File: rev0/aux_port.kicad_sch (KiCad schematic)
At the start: 21 parts, among them IC1 ECP5-BGA256, U11 USB3343-CP

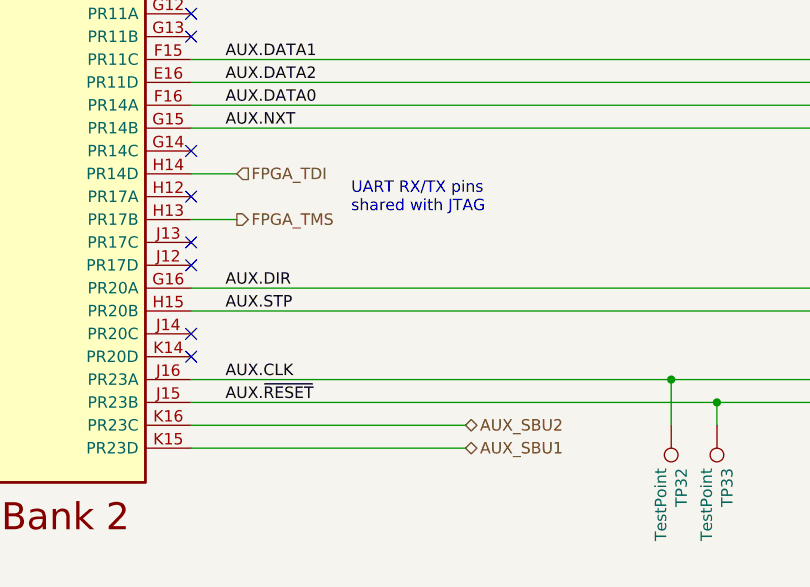
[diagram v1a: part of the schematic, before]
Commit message: hardware: replace power input diodes
- provide input selection capability with FETs
- reduce reverse leakage current
- provide overvoltage protection
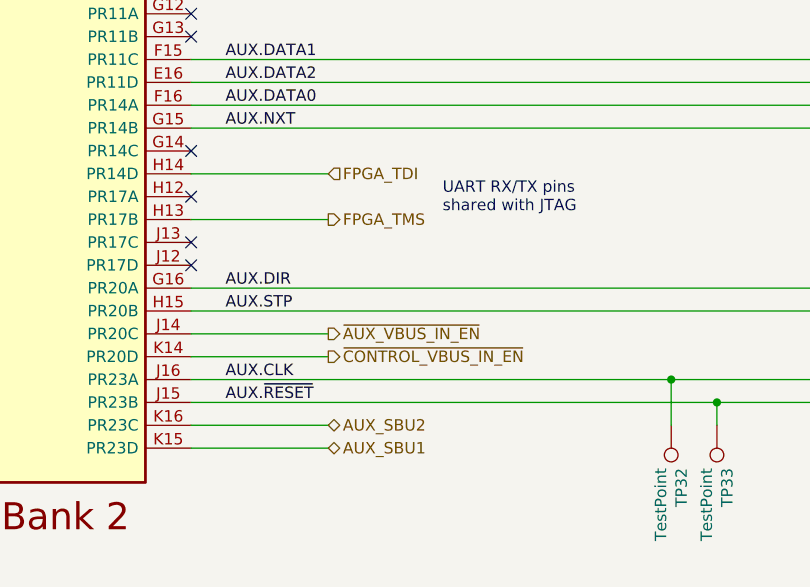
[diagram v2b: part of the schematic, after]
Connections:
- net ~{AUX_VBUS_IN_EN}: now reaches IC1.J14 (PR20C)
- net ~{CONTROL_VBUS_IN_EN}: now reaches IC1.K14 (PR20D)
- no-connect marks 14 -> 12
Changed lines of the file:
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@@
   (no_connect (at 59.69 95.25))
   (no_connect (at 59.69 115.57))
-  (no_connect (at 59.69 130.81))
   (no_connect (at 59.69 72.39))
   (no_connect (at 59.69 120.65))
   (no_connect (at 59.69 82.55))
-  (no_connect (at 59.69 133.35))
   (no_connect (at 59.69 123.19))
   (no_connect (at 227.33 87.63))
@@
     (stroke (width 0) (type default) (color 0 0 0 0))
   )
-  (wire (pts (xy 90.17 140.97) (xy 59.69 140.97))
+  (wire (pts (xy 74.93 140.97) (xy 59.69 140.97))
     (stroke (width 0) (type default) (color 0 0 0 0))
   )
@@
     (stroke (width 0) (type default) (color 0 0 0 0))
   )
+  (wire (pts (xy 74.93 133.35) (xy 59.69 133.35))
+    (stroke (width 0) (type default) (color 0 0 0 0))
+  )
   (bus (pts (xy 148.59 82.55) (xy 148.59 83.82))
     (stroke (width 0) (type default) (color 0 0 0 0))
@@
     (stroke (width 0) (type default) (color 0 0 0 0))
   )
-  (wire (pts (xy 59.69 118.11) (xy 64.77 118.11))
+  (wire (pts (xy 59.69 118.11) (xy 74.93 118.11))
     (stroke (width 0) (type default) (color 0 0 0 0))
   )
@@
     (stroke (width 0) (type default) (color 0 0 0 0))
   )
-  (wire (pts (xy 59.69 143.51) (xy 90.17 143.51))
+  (wire (pts (xy 59.69 143.51) (xy 74.93 143.51))
     (stroke (width 0) (type default) (color 0 0 0 0))
   )
@@
     (stroke (width 0) (type default) (color 0 0 0 0))
   )
+  (wire (pts (xy 59.69 130.81) (xy 74.93 130.81))
+    (stroke (width 0) (type default) (color 0 0 0 0))
+  )
   (wire (pts (xy 238.76 135.89) (xy 238.76 138.43))
     (stroke (width 0) (type default) (color 0 0 0 0))
@@
     (stroke (width 0) (type default) (color 0 0 0 0))
   )
-  (wire (pts (xy 64.77 113.03) (xy 59.69 113.03))
+  (wire (pts (xy 74.93 113.03) (xy 59.69 113.03))
     (stroke (width 0) (type default) (color 0 0 0 0))
   )
@@
     (stroke (width 0) (type default) (color 0 0 0 0))
   )
-  (text "UART RX/TX pins\nshared with JTAG" (at 77.47 117.475 0)
+  (text "UART RX/TX pins\nshared with JTAG" (at 87.63 117.475 0)
     (effects (font (size 1.27 1.27)) (justify left bottom))
   )
@@
     (effects (font (size 1.27 1.27)) (justify right bottom))
   )
-  (hierarchical_label "FPGA_TMS" (shape output) (at 64.77 118.11 0)
+  (hierarchical_label "FPGA_TMS" (shape output) (at 74.93 118.11 0)
     (effects (font (size 1.27 1.27)) (justify left))
   )
@@
     (effects (font (size 1.27 1.27)) (justify left))
   )
-  (hierarchical_label "AUX_SBU1" (shape bidirectional) (at 90.17 143.51 0)
+  (hierarchical_label "AUX_SBU1" (shape bidirectional) (at 74.93 143.51 0)
+    (effects (font (size 1.27 1.27)) (justify left))
+  )
+  (hierarchical_label "~{AUX_VBUS_IN_EN}" (shape output) (at 74.93 130.81 0)
     (effects (font (size 1.27 1.27)) (justify left))
   )
@@
     (effects (font (size 1.27 1.27)) (justify left))
   )
-  (hierarchical_label "AUX_SBU2" (shape bidirectional) (at 90.17 140.97 0)
-    (effects (font (size 1.27 1.27)) (justify left))
-  )
-  (hierarchical_label "FPGA_TDI" (shape input) (at 64.77 113.03 0)
-    (effects (font (size 1.27 1.27)) (justify left))
-  )
+  (hierarchical_label "AUX_SBU2" (shape bidirectional) (at 74.93 140.97 0)
+    (effects (font (size 1.27 1.27)) (justify left))
+  )
+  (hierarchical_label "~{CONTROL_VBUS_IN_EN}" (shape output) (at 74.93 133.35 0)
+    (effects (font (size 1.27 1.27)) (justify left))
+  )
+  (hierarchical_label "FPGA_TDI" (shape input) (at 74.93 113.03 0)
+    (effects (font (size 1.27 1.27)) (justify left))
+  )

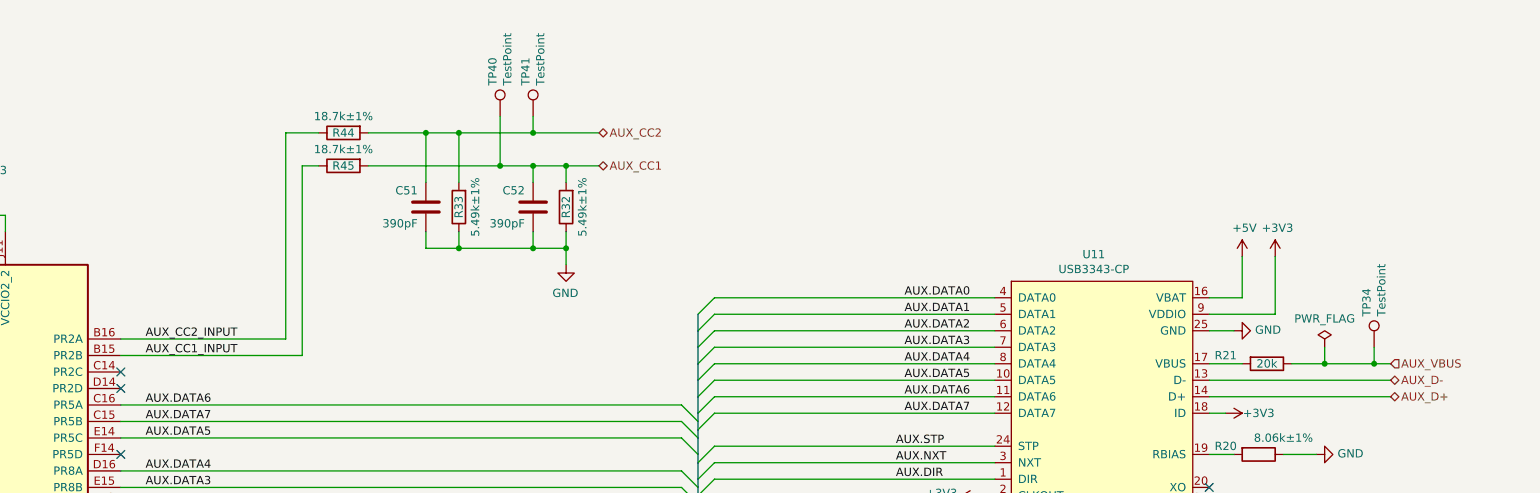
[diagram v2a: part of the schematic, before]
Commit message: hardware: add Aux port Type-C controller
replaces rudimentary CC pin input
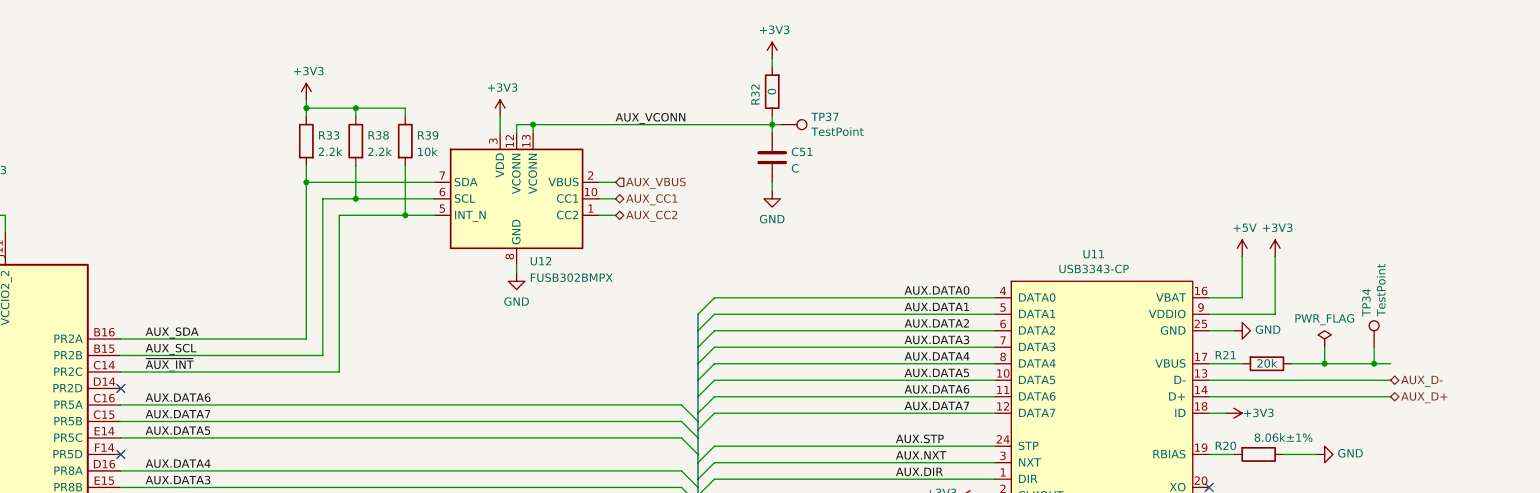
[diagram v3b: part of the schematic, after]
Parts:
- removed C52: 390pF, Capacitor_SMD:C_0402_1005Metric, symbol Device:C
- removed R44, R45: 18.7k±1%, Resistor_SMD:R_0402_1005Metric, symbol Device:R
- removed TP40, TP41: TestPoint, TestPoint:TestPoint_Pad_D1.0mm, symbol Connector:TestPoint
- added R38: 2.2k, Resistor_SMD:R_0402_1005Metric, symbol Device:R
- added R39: 10k, Resistor_SMD:R_0402_1005Metric, symbol Device:R
- added TP37: TestPoint, TestPoint:TestPoint_Pad_D1.0mm, symbol Connector:TestPoint
- added U12: FUSB302BMPX, Package_DFN_QFN:WQFN-14-1EP_2.5x2.5mm_P0.5mm_EP1.45x1.45mm, symbol Interface_USB:FUSB302BMPX
- C51: value 390pF -> C; Part Number GENERIC-CAP-0402-390pF -> (none); Substitution any equivalent -> (none)
- R32: value 5.49k±1% -> 0; Manufacturer Panasonic -> (none); Part Number ERJ-2RKF5491X -> GENERIC-RES-0402-0
- R33: value 5.49k±1% -> 2.2k; Manufacturer Panasonic -> (none); Part Number ERJ-2RKF5491X -> GENERIC-RES-0402-2.2K
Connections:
- net +3V3: now also R32.2, R33.1, R38.1, R39.1, U12.3 (VDD), U12.4 (VDD)
- net AUX_CC1: now also U12.10 (CC1), U12.11 (CC1); no longer R32.2
- net AUX_CC2: now also U12.1 (CC2), U12.14 (CC2); no longer C51.1, R33.2
- net AUX_VBUS: now also U12.2 (VBUS); no longer R21.1, TP34.1
- net GND: now also U12.15 (GND), U12.8 (GND), U12.9 (GND); no longer R32.1, R33.1
- net ~{AUX_INT}: now reaches IC1.C14 (PR2C)
- net ~{AUX_INT}: now also R39.2, U12.5 (INT_N)
- net AUX_CC1_INPUT renamed AUX_SCL
- net AUX_SCL: now also R38.2, U12.6 (SCL)
- net AUX_CC2_INPUT renamed AUX_SDA
- net AUX_SDA: now also R33.2, U12.7 (SDA)
- new net: R21.1, TP34.1
- new net AUX_VCONN: C51.1, R32.1, TP37.1, U12.12 (VCONN), U12.13 (VCONN)
- no-connect marks 12 -> 11

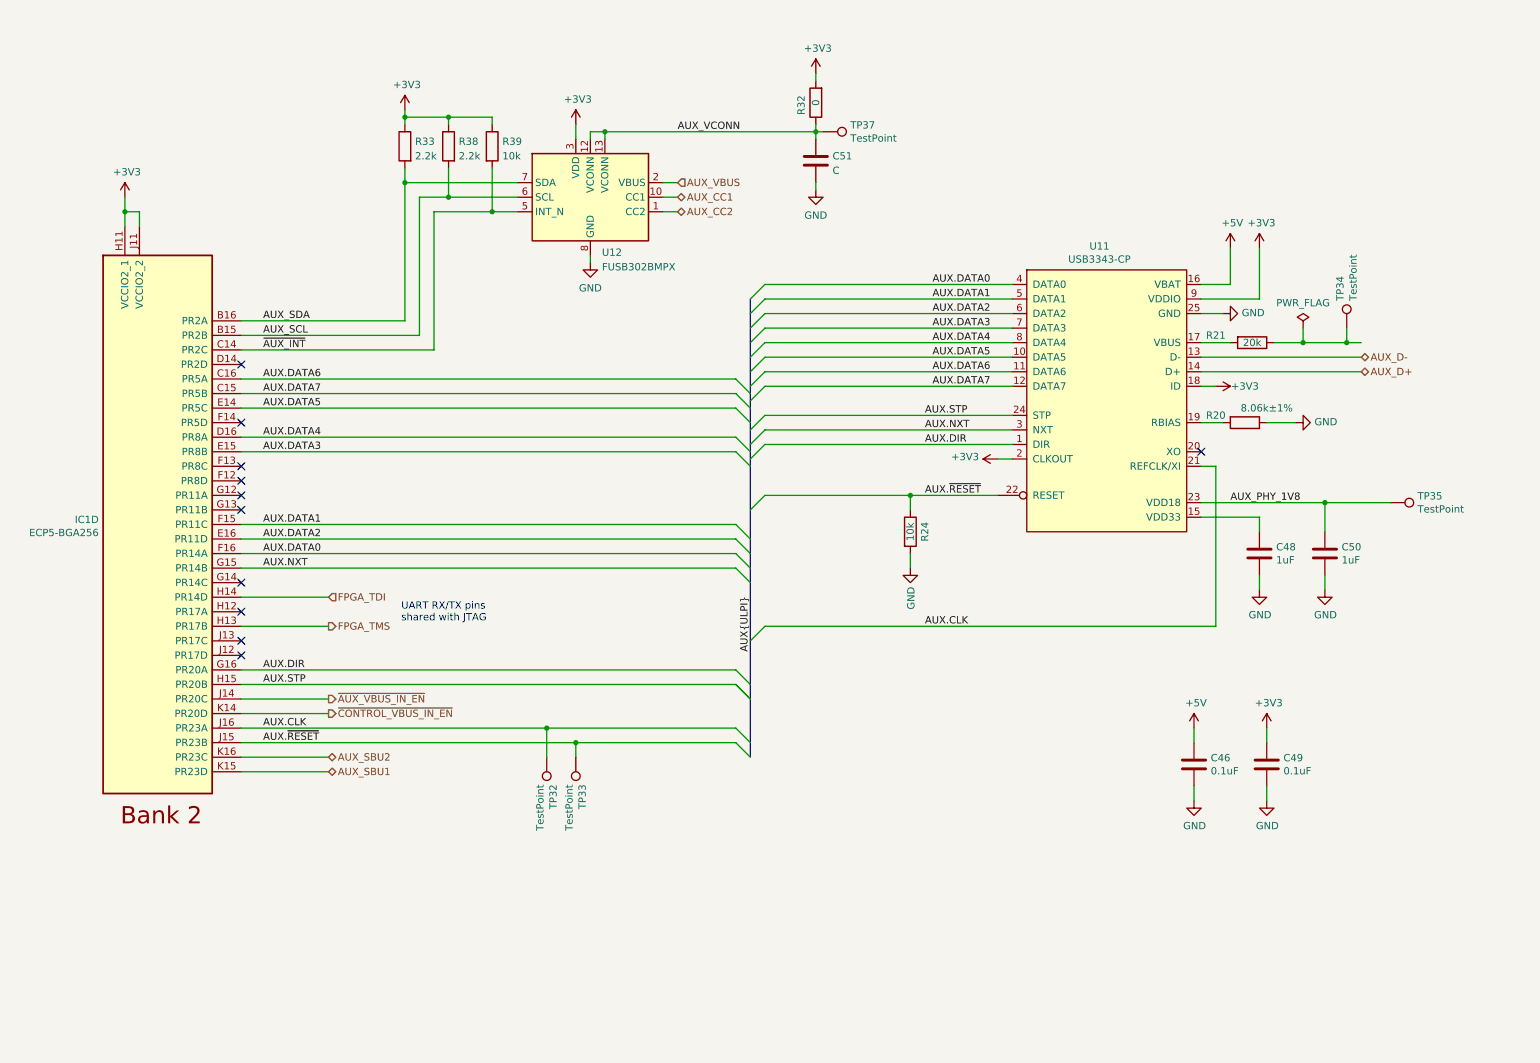
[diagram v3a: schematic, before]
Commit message: hardware: simplify Control port Type-C connections
- remove CC/FPGA connections to ensure correct Rd is reliably present
- remove SBU/FPGA connections to avoid need for ESD protection

We provide CC and SBU pin access on the Target and Aux port. They are
not necessary on the Control port. Simplification ensures reliability.
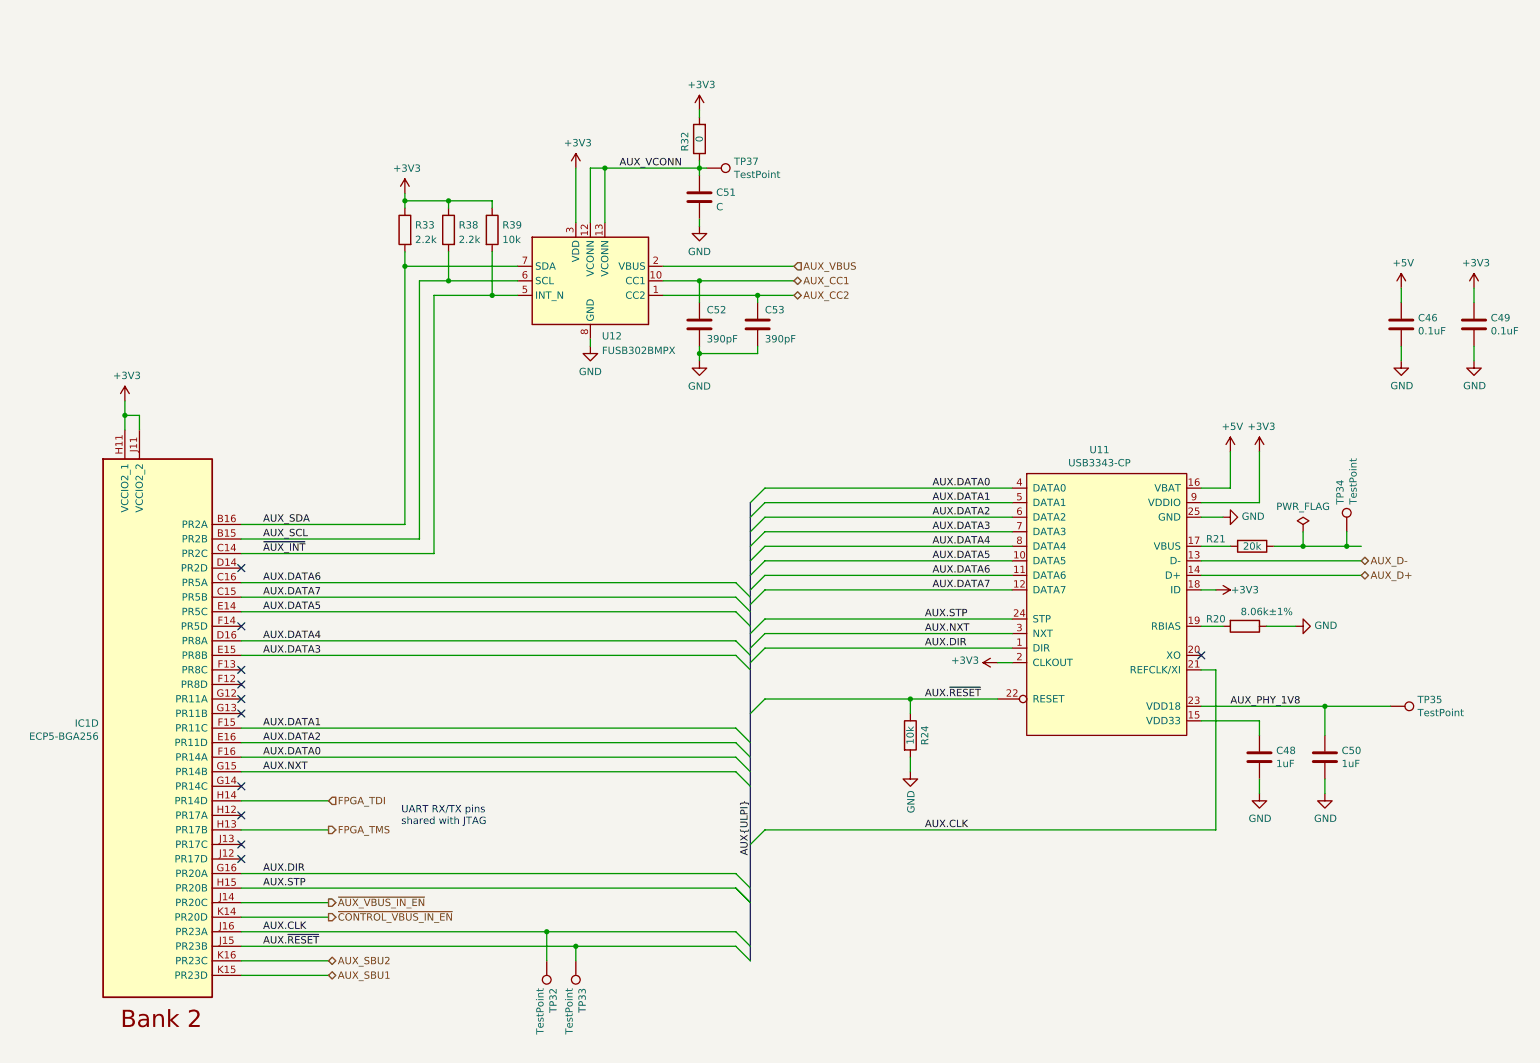
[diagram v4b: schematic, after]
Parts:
- added C52, C53: 390pF, Capacitor_SMD:C_0402_1005Metric, symbol Device:C
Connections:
- net AUX_CC1: now also C52.1
- net AUX_CC2: now also C53.1
- net GND: now also C52.2, C53.2
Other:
- moved on the sheet: C46, C48, C49, C50, C51, IC1D, R20, R21, R24, R32, R33, R38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
